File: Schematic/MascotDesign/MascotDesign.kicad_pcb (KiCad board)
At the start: 2 copper layers, 46 parts, among them J1 Charger input, J2 PI power USB, J3 LCD power USB, J4 LCD power USB, J5 Audio in, J6 Audio in, J8 Potentiometer, J9 Speaker 8R, SW1 Main power cutoff, U3 TPA3116D2DAD

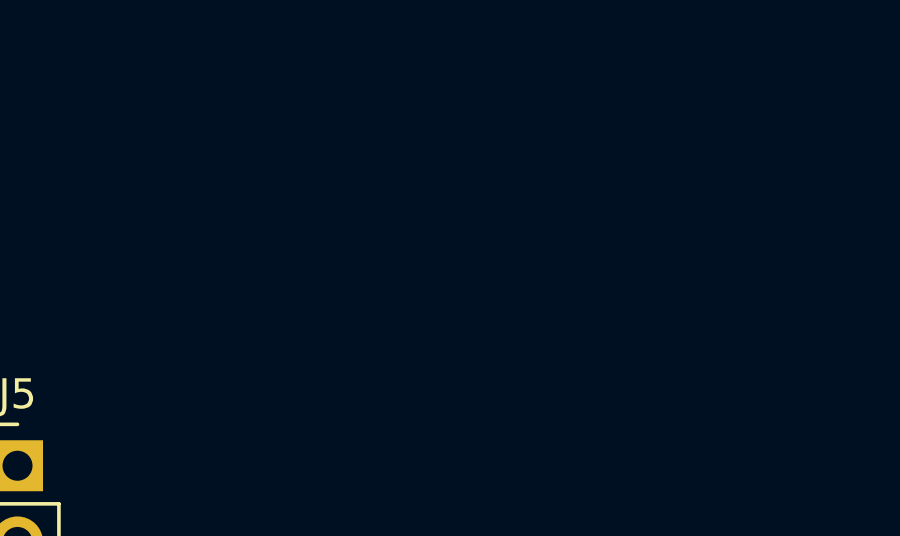
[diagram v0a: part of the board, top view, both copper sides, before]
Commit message: Work on CAD and schematics
Got most of the components modeled for reference, now arranging them and creating brackets
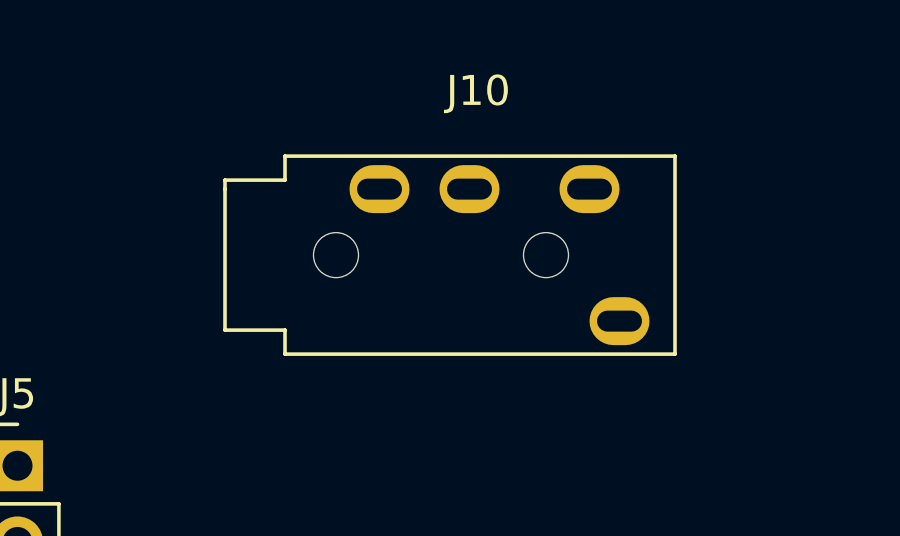
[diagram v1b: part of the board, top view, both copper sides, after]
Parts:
- added J10: AudioJack4, My_Library:PJ-320A, F.Cu at (143.8, 36.7)
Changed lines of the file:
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@@
 	(net 37 "unconnected-(J4-Pin_1-Pad1)")
 	(net 38 "unconnected-(J4-Pin_2-Pad2)")
+	(net 39 "unconnected-(J10-PadR2)")
+	(net 40 "unconnected-(J10-PadR1)")
 	(footprint "Resistor_THT:R_Axial_DIN0207_L6.3mm_D2.5mm_P7.62mm_Horizontal"
 		(layer "F.Cu")
@@
 		)
 	)
+	(footprint "My_Library:PJ-320A"
+		(layer "F.Cu")
+		(at 143.822 36.748)
+		(property "Reference" "J10"
+			(at 8.4455 -3.269 0)
+			(layer "F.SilkS")
+			(effects
+				(font
+					(size 1 1)
+					(thickness 0.15)
+				)
+			)
+		)
+		(property "Value" "AudioJack4"
+			(at 8.4455 -4.539 0)
+			(layer "F.Fab")
+			(effects
+				(font
+					(size 1 1)
+					(thickness 0.15)
+				)
+			)
+		)
+		(property "Datasheet" ""
+			(at 0 0 0)
+			(layer "F.Fab")
+			(hide yes)
+			(effects
+				(font
+					(size 1.27 1.27)
+					(thickness 0.15)
+				)
+			)
+		)
+		(property "Description" "Audio Jack, 4 Poles (TRRS)"
+			(at 0 0 0)
+			(layer "F.Fab")
+			(hide yes)
+			(effects
+				(font
+					(size 1.27 1.27)
+					(thickness 0.15)
+				)
+			)
+		)
+		(property ki_fp_filters "Jack*")
+		(sheetname "/Amplifier/")
+		(sheetfile "Amplifier_Circuit.kicad_sch")
+		(attr through_hole)
+		(fp_line
+			(start 0 -0.3)
+			(end 2 -0.3)
+			(stroke
+				(width 0.12)
+				(type solid)
+			)
+			(layer "F.SilkS")
+		)
+		(fp_line
+			(start 0 0)
+			(end 0 -0.3)
+			(stroke
+				(width 0.12)
+				(type solid)
+			)
+			(layer "F.SilkS")
+		)
+		(fp_line
+			(start 0 0)
+			(end 0 4.7)
+			(stroke
+				(width 0.12)
+				(type solid)
+			)
+			(layer "F.SilkS")
+		)
+		(fp_line
+			(start 0 4.7)
+			(end 2 4.7)
+			(stroke
+				(width 0.12)
+				(type solid)
+			)
+			(layer "F.SilkS")
+		)
+		(fp_line
+			(start 2 -1.1)
+			(end 15 -1.1)
+			(stroke
+				(width 0.12)
+				(type solid)
+			)
+			(layer "F.SilkS")
+		)
+		(fp_line
+			(start 2 -0.3)
+			(end 2 -1.1)
+			(stroke
+				(width 0.12)
+				(type solid)
+			)
+			(layer "F.SilkS")
+		)
+		(fp_line
+			(start 2 4.7)
+			(end 2 5.5)
+			(stroke
+				(width 0.12)
+				(type solid)
+			)
+			(layer "F.SilkS")
+		)
+		(fp_line
+			(start 2 5.5)
+			(end 15 5.5)
+			(stroke
+				(width 0.12)
+				(type solid)
+			)
+			(layer "F.SilkS")
+		)
+		(fp_line
+			(start 15 -1.1)
+			(end 15 5.5)
+			(stroke
+				(width 0.12)
+				(type solid)
+			)
+			(layer "F.SilkS")
+		)
+		(pad "" np_thru_hole circle
+			(at 3.7 2.2)
+			(size 1.5 1.5)
+			(drill 1.5)
+			(layers "*.Cu")
+		)
+		(pad "" np_thru_hole circle
+			(at 10.7 2.2)
+			(size 1.5 1.5)
+			(drill 1.5)
+			(layers "*.Cu")
+		)
+		(pad "R1" thru_hole oval
+			(at 12.15 0)
+			(size 2 1.6)
+			(drill oval 1.5 0.7)
+			(layers "*.Cu" "*.Mask")
+			(remove_unused_layers no)
+			(net 40 "unconnected-(J10-PadR1)")
+			(pintype "passive+no_connect")
+		)
+		(pad "R2" thru_hole oval
+			(at 8.15 0)
+			(size 2 1.6)
+			(drill oval 1.5 0.7)
+			(layers "*.Cu" "*.Mask")
+			(remove_unused_layers no)
+			(net 39 "unconnected-(J10-PadR2)")
+			(pintype "passive+no_connect")
+		)
+		(pad "S" thru_hole oval
+			(at 5.15 0)
+			(size 2 1.6)
+			(drill oval 1.5 0.7)
+			(layers "*.Cu" "*.Mask")
+			(remove_unused_layers no)
+			(net 4 "Net-(J5-Pin_2)")
+			(pintype "passive")
+		)
+		(pad "T" thru_hole oval
+			(at 13.15 4.4)
+			(size 2 1.6)
+			(drill oval 1.5 0.7)
+			(layers "*.Cu" "*.Mask")
+			(remove_unused_layers no)
+			(net 1 "Net-(J5-Pin_1)")
+			(pintype "passive")
+		)
+		(embedded_fonts no)
+	)
 	(footprint "Capacitor_THT:CP_Radial_D5.0mm_P2.50mm"

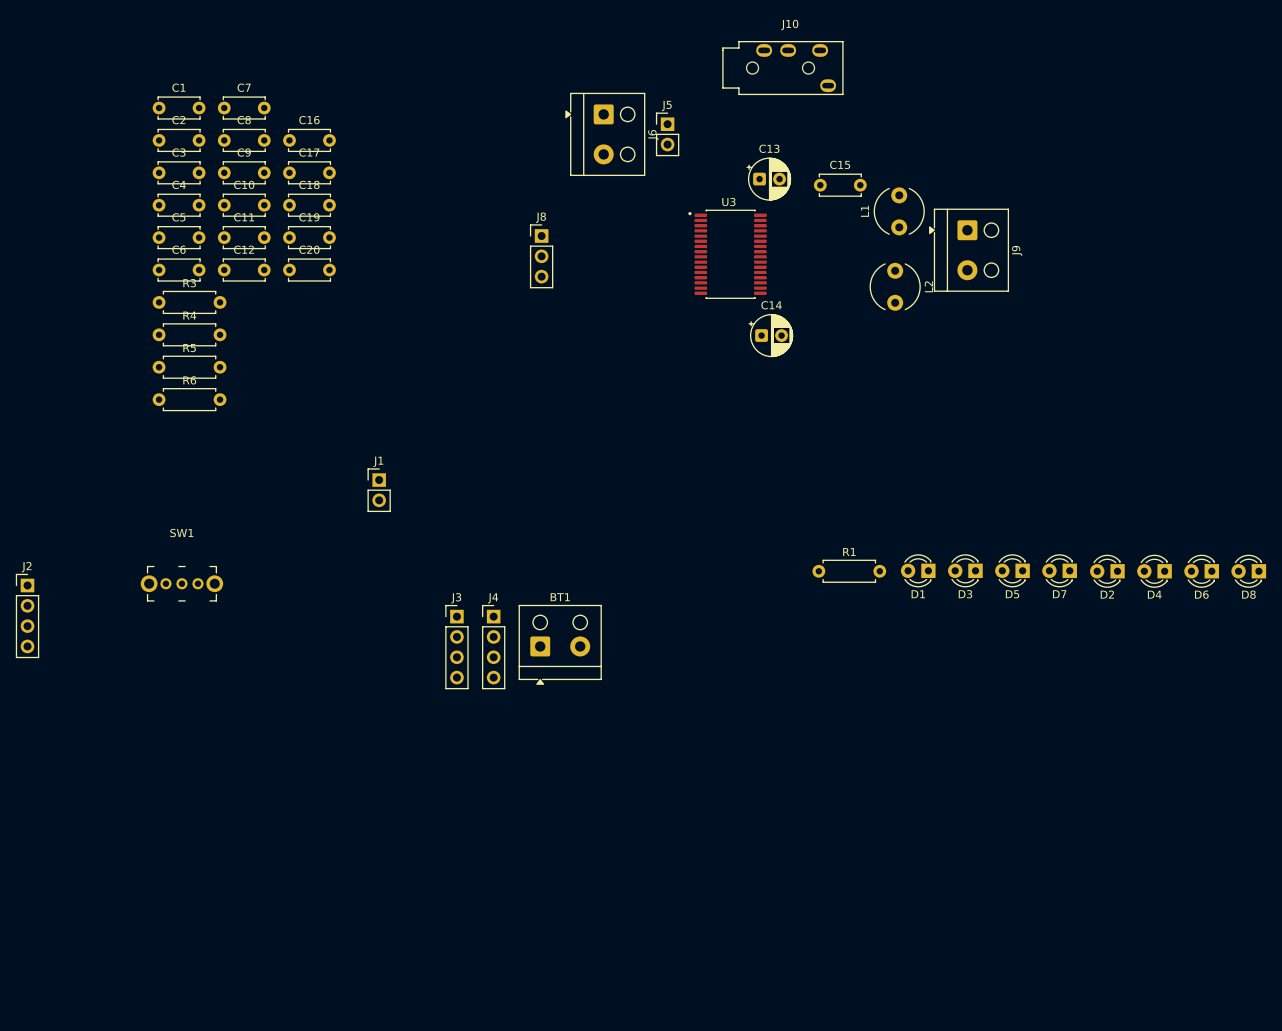
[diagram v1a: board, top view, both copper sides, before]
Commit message: Do PCB layout
I need to check our cap footprints to make sure we got the right ones.
Other than that, the PCB should be mostly routed.
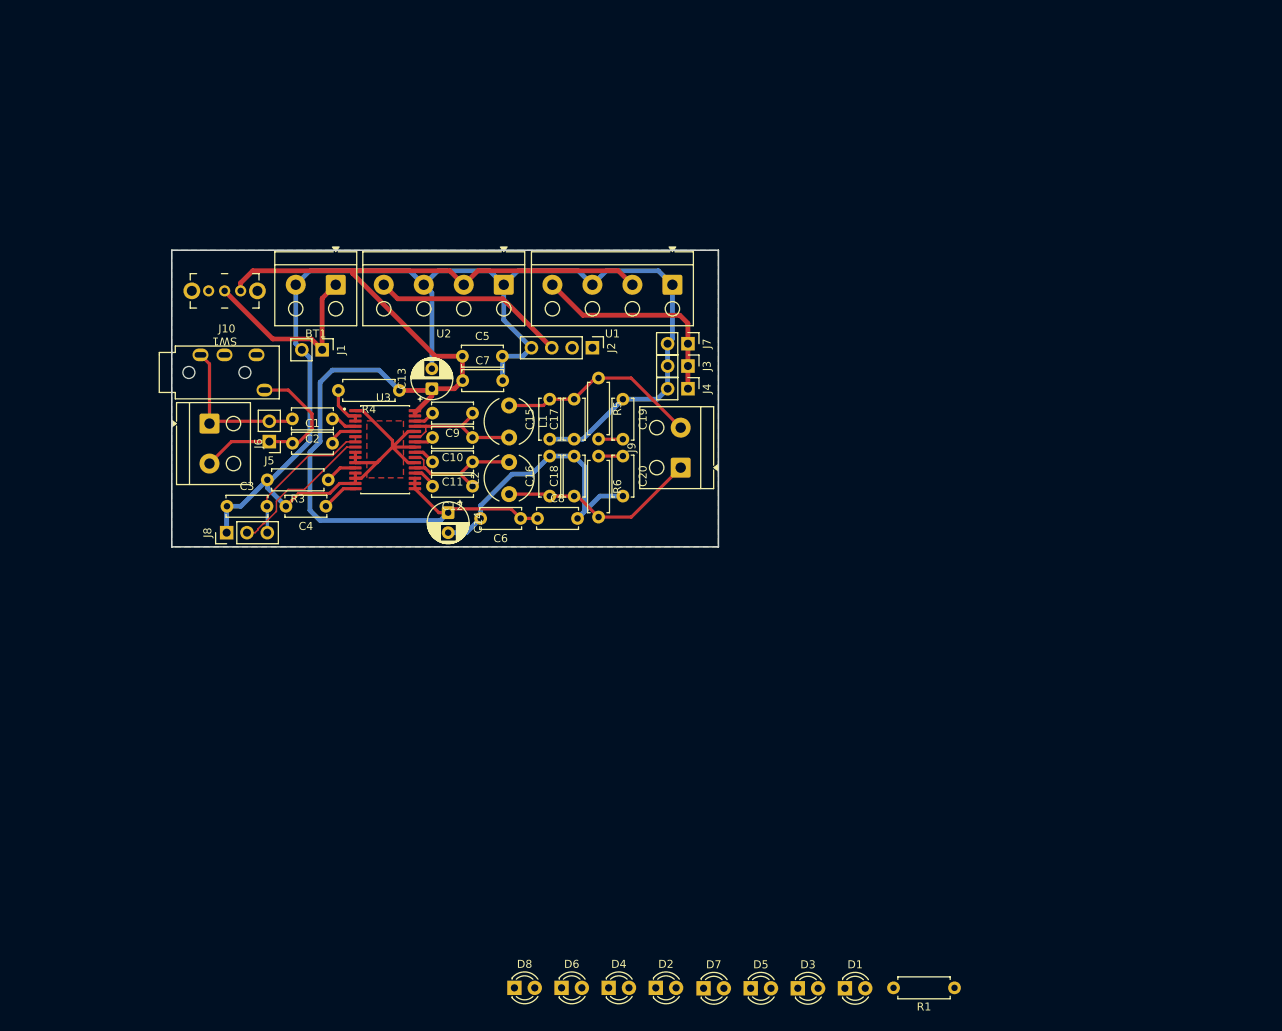
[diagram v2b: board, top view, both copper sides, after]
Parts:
- added J7: LED Connector, Connector_PinHeader_2.54mm:PinHeader_1x02_P2.54mm_Vertical, F.Cu at (139.4, 73.4)
- added U1: Generic_Buck_Regulator, TerminalBlock_RND:TerminalBlock_RND_205-00003_1x04_P5.00mm_Horizontal, F.Cu at (137.5, 66.0)
- added U2: Generic_Buck_Regulator, TerminalBlock_RND:TerminalBlock_RND_205-00003_1x04_P5.00mm_Horizontal, F.Cu at (116.4, 66.0)
- J3, J4: footprint Connector_PinHeader_2.54mm:PinHeader_1x04_P2.54mm_Vertical -> Connector_PinHeader_2.54mm:PinHeader_1x02_P2.54mm_Vertical
- moved D8 106.6 mm to (117.8, 153.9), turned to 0 degrees
- moved D6 96.5 mm to (123.7, 153.9), turned to 0 degrees
- moved D4 86.8 mm to (129.5, 153.9), turned to 0 degrees
- moved J10 80.1 mm to (73.4, 74.8)
- moved D2 77.7 mm to (135.4, 153.9), turned to 0 degrees
- moved J2 76.6 mm to (127.5, 73.9), turned to -90 degrees
- moved D7 69.4 mm to (141.4, 154.0), turned to 0 degrees
- moved J5 63.7 mm to (87.1, 85.6), turned to 180 degrees
- moved J6 62.6 mm to (79.6, 83.4)
- moved D5 62.3 mm to (147.3, 154.0), turned to 0 degrees
- moved C8 61.4 mm to (120.7, 95.2)
- moved D3 56.7 mm to (153.2, 154.0), turned to 0 degrees
- moved L2 55.8 mm to (117.1, 92.2), turned to 90 degrees
- moved R6 55.4 mm to (128.3, 87.5), turned to -90 degrees
- moved C16 55.1 mm to (122.2, 92.5), turned to 90 degrees
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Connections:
- BT1 pad 2: 12V SWITCHED -> GND
- C1 pad 1: Net-(U3-RINN) -> Net-(J5-Pin_1)
- C1 pad 2: Net-(J5-Pin_1) -> Net-(U3-RINN)
- C10 pad 1: Net-(U3-BSNR) -> Net-(U3-OUTNR)
- C10 pad 2: Net-(U3-OUTNR) -> Net-(U3-BSNR)
- C12 pad 1: Net-(U3-BSNL) -> Net-(U3-OUTNL)
- C12 pad 2: Net-(U3-OUTNL) -> Net-(U3-BSNL)
- C13 pad 2: 12V SWITCHED -> GND
- C14 pad 2: 12V SWITCHED -> GND
- C15 pad 1: 12V SWITCHED -> GND
- C15 pad 2: Net-(J9-Pin_1) -> Net-(J9-Pin_2)
- C16 pad 1: Net-(J9-Pin_2) -> Net-(J9-Pin_1)
- C16 pad 2: 12V SWITCHED -> GND
- C17 pad 1: 12V SWITCHED -> GND
- C17 pad 2: Net-(J9-Pin_1) -> Net-(J9-Pin_2)
- C18 pad 1: Net-(J9-Pin_2) -> Net-(J9-Pin_1)
- C18 pad 2: 12V SWITCHED -> GND
- C19 pad 1: 12V SWITCHED -> GND
- C20 pad 2: 12V SWITCHED -> GND
- C3 pad 1: 12V SWITCHED -> GND
- C4 pad 2: 12V SWITCHED -> GND
- C5 pad 2: 12V SWITCHED -> GND
- C6 pad 2: 12V SWITCHED -> GND
- C7 pad 2: 12V SWITCHED -> GND
- C8 pad 2: 12V SWITCHED -> GND
- D8 pad 1: 12V SWITCHED -> GND
- J1 pad 2: 12V SWITCHED -> GND
- J2 pad 4: 12V SWITCHED -> GND
- J3 pad 1: unconnected-(J3-Pin_1-Pad1) -> LCD 5v5
- J3 pad 2: unconnected-(J3-Pin_2-Pad2) -> GND
- J4 pad 1: unconnected-(J4-Pin_1-Pad1) -> LCD 5v5
- J4 pad 2: unconnected-(J4-Pin_2-Pad2) -> GND
- J6 pad 1: Net-(J5-Pin_1) -> Net-(J5-Pin_2)
- J6 pad 2: Net-(J5-Pin_2) -> Net-(J5-Pin_1)
- J8 pad 1: /Amplifier/Gain adjust supply -> GND
- J8 pad 2: 12V SWITCHED -> /Amplifier/Gain adjust supply
- L1 pad 1: Net-(J9-Pin_1) -> Net-(J9-Pin_2)
- L2 pad 1: Net-(J9-Pin_2) -> Net-(J9-Pin_1)
- R3 pad 2: 12V SWITCHED -> GND
- R5 pad 1: Net-(J9-Pin_1) -> Net-(J9-Pin_2)
- R6 pad 2: Net-(J9-Pin_2) -> Net-(J9-Pin_1)
- U3 pad 1: 12V SWITCHED -> GND
- U3 pad 10: 12V SWITCHED -> GND
- U3 pad 11: 12V SWITCHED -> GND
- U3 pad 13: 12V SWITCHED -> GND
- U3 pad 14: 12V SWITCHED -> GND
- U3 pad 15: 12V SWITCHED -> GND
- U3 pad 22: 12V SWITCHED -> GND
- U3 pad 25: 12V SWITCHED -> GND
- U3 pad 28: 12V SWITCHED -> GND
- U3 pad 9: 12V SWITCHED -> GND
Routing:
- net GND: track 0.00 -> 227.5 mm
- net 12V SWITCHED: track 0.00 -> 153.2 mm
- net LCD 5v5: track 0.00 -> 27.1 mm
- net Net-(J9-Pin_2): track 0.00 -> 25.4 mm
- net Net-(J9-Pin_1): track 0.00 -> 25.2 mm
- net /Power supply/PI 5v5: track 0.00 -> 24.3 mm
- net +12V: track 0.00 -> 24.1 mm
- net Net-(J5-Pin_1): track 0.00 -> 23.7 mm
- net Net-(J5-Pin_2): track 0.00 -> 20.2 mm
- net /Amplifier/Power limit input: track 0.00 -> 19.0 mm
- net /Amplifier/Gain adjust supply: track 0.00 -> 18.8 mm
- net Net-(U3-OUTNL): track 0.00 -> 17.2 mm
- net Net-(U3-OUTNR): track 0.00 -> 16.9 mm
- net Net-(U3-FAULTZ): track 0.00 -> 5.21 mm
- net Net-(U3-SYNC): track 0.00 -> 4.60 mm
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- added copper zone on B.Cu, net GND
- added copper zone on F.Cu, net GND
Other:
- board outline added: 68.3 x 37.1 mm

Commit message: update PCB and mounting brackets
give PCB the correct footprints for the parts we have and add more mounting brackets for the 3D model
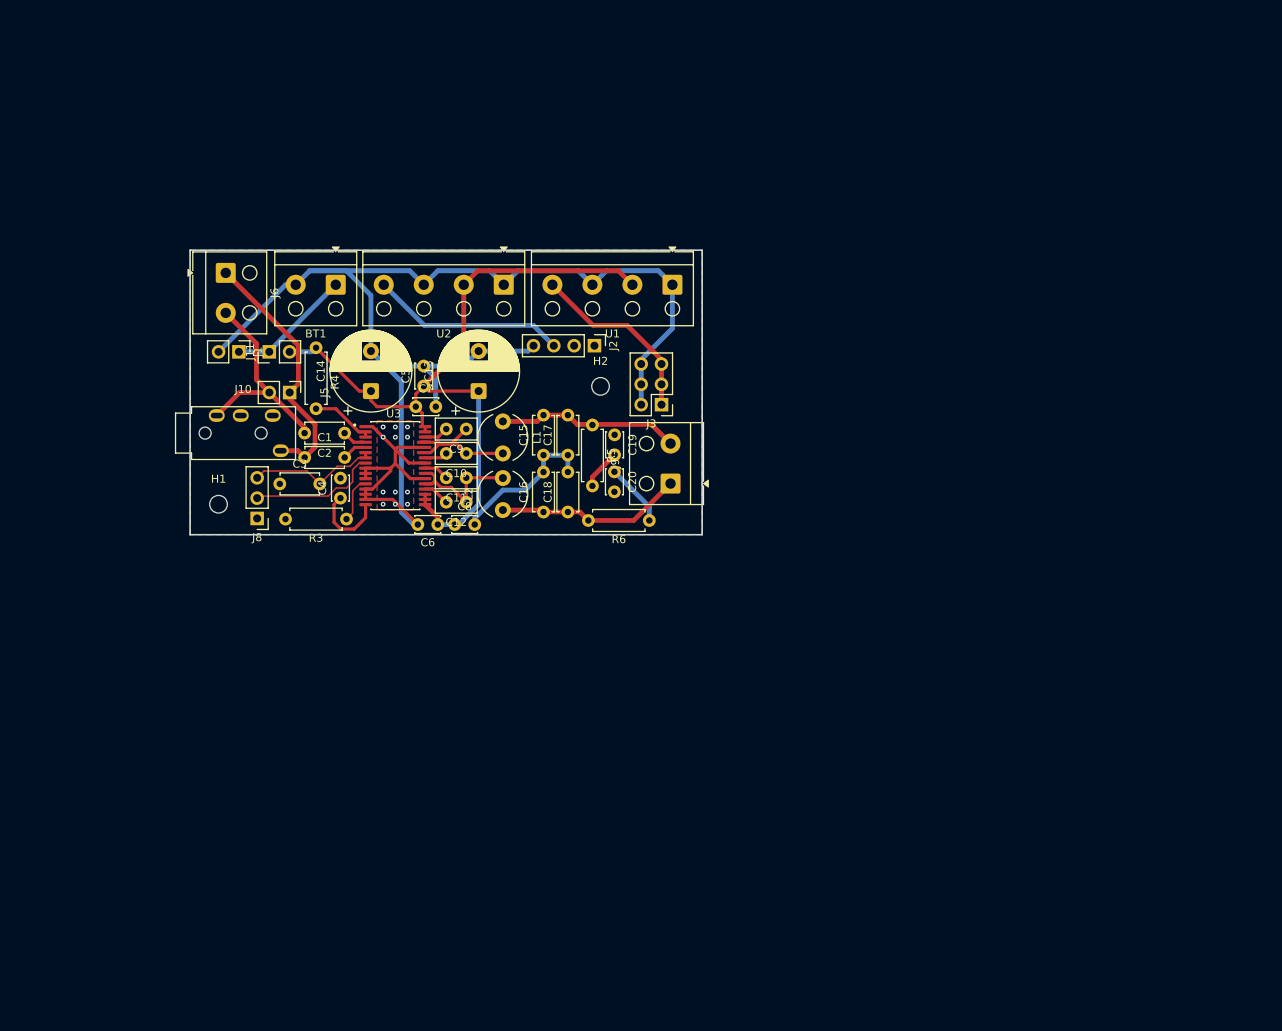
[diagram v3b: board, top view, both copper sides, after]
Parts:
- removed D1, D2, D3, D4, D5, D6, D7, D8: LED, LED_THT:LED_D3.0mm
- removed J4: LCD power USB, Connector_PinHeader_2.54mm:PinHeader_1x02_P2.54mm_Vertical
- removed J7: LED Connector, Connector_PinHeader_2.54mm:PinHeader_1x02_P2.54mm_Vertical
- removed R1: R100, Resistor_THT:R_Axial_DIN0207_L6.3mm_D2.5mm_P7.62mm_Horizontal
- removed SW1: Main power cutoff, My_Library:SK12D07VG4
- added H1: MountingHole, MountingHole:MountingHole_2.2mm_M2, F.Cu at (80.8, 93.5)
- added H2: MountingHole, MountingHole:MountingHole_2.2mm_M2, F.Cu at (128.5, 78.7)
- added J11: Main power cutoff (soldered switch), Connector_PinHeader_2.54mm:PinHeader_1x02_P2.54mm_Vertical, F.Cu at (87.1, 74.4)
- C1, C15, C16, C17, C18, C2, C3: footprint Capacitor_THT:C_Disc_D5.0mm_W2.5mm_P5.00mm -> Capacitor_THT:C_Disc_D4.7mm_W2.5mm_P5.00mm
- C10, C11, C12, C9: footprint Capacitor_THT:C_Disc_D5.0mm_W2.5mm_P5.00mm -> Capacitor_THT:C_Disc_D5.0mm_W2.5mm_P2.50mm
- C13, C14: footprint Capacitor_THT:CP_Radial_D5.0mm_P2.50mm -> Capacitor_THT:CP_Radial_D10.0mm_P5.00mm
- C19, C20, C4, C5, C6, C7, C8: footprint Capacitor_THT:C_Disc_D5.0mm_W2.5mm_P5.00mm -> Capacitor_THT:C_Disc_D3.0mm_W2.0mm_P2.50mm
- J3: value LCD power USB -> LCD LED Power; footprint Connector_PinHeader_2.54mm:PinHeader_1x02_P2.54mm_Vertical -> Connector_PinHeader_2.54mm:PinHeader_2x03_P2.54mm_Vertical
- moved J6 18.9 mm to (81.7, 64.6)
- moved C14 18.0 mm to (99.8, 79.3), turned to 90 degrees
- moved R4 11.7 mm to (93.0, 73.9), turned to -90 degrees
- moved J1 10.4 mm to (83.3, 74.4)
- moved C6 10.4 mm to (108.2, 96.0)
- moved C8 10.4 mm to (110.3, 96.0)
- moved R6 10.2 mm to (134.6, 95.5), turned to 180 degrees
- moved J10 7.85 mm to (75.4, 82.4)
- moved C3 7.17 mm to (88.4, 90.9)
- moved C7 6.71 mm to (105.4, 81.3)
- moved J5 6.64 mm to (89.7, 79.5), turned to -90 degrees
- moved C5 6.10 mm to (106.4, 78.7), turned to 90 degrees
- moved R5 5.91 mm to (127.5, 83.6)
- moved J3 5.85 mm to (136.1, 81.0), turned to 180 degrees
- moved C13 5.85 mm to (113.3, 79.3)
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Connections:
- J6 pad 1: Net-(J5-Pin_2) -> Net-(J5-Pin_1)
- J6 pad 2: Net-(J5-Pin_1) -> Net-(J5-Pin_2)
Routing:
- net 12V SWITCHED: track 153.2 -> 95.4 mm
- net GND: track 227.5 -> 208.0 mm, vias 0 -> 12
- net Net-(J5-Pin_1): track 23.7 -> 32.5 mm
- net +12V: track 24.1 -> 15.4 mm
- net Net-(J5-Pin_2): track 20.2 -> 26.9 mm
- net Net-(U3-SYNC): track 4.60 -> 9.87 mm
- net Net-(C20-Pad1): track 3.04 -> 7.89 mm
- net LCD 5v5: track 27.1 -> 23.1 mm
- net Net-(U3-FAULTZ): track 5.21 -> 8.04 mm
- net Net-(J9-Pin_2): track 25.4 -> 22.8 mm
- net /Amplifier/Power limit input: track 19.0 -> 16.6 mm
- net /Amplifier/Gain adjust supply: track 18.8 -> 16.4 mm
- net Net-(C19-Pad2): track 3.06 -> 5.04 mm
- net Net-(U3-MUTE): track 4.01 -> 5.82 mm
- net Net-(J9-Pin_1): track 25.2 -> 23.4 mm
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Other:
- board size 68.3 x 37.1 mm -> 64 x 35.6 mm
